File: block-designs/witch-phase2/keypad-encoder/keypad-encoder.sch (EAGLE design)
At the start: 70 parts, among them IC1 74AHC1G14DBV, IC2 74AHC1G14DBV, IC3 74AHC1G14DBV, IC4 74AHC1G14DBV, IC5 74AHC1G14DBV

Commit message: completed schematic with basic pcb layout
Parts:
- removed D26, D28, D30, D31, D32, D33, D34: (no value), SparkFun-DiscreteSemi:DIODEPTH
- removed JP1: (no value), pinhead:PINHD-1X18
- added D1, D2: (no value), SparkFun-DiscreteSemi:DIODEPTH
- added IC6: 74LVC1G17DBV, 74xx-little-us:74LVC1G17DBV
- added IC7: 74LVC1G14DBV, 74xx-little-us:74LVC1G14DBV
- added JP2: (no value), pinhead:PINHD-1X10
- added JP3: (no value), pinhead:PINHD-1X18
- added R17, R18, R19, R20, R21: 1k, resistor:R-US_R0805
- C1, C10, C11, C12, C13, C14, C15, C16, C2, C3, C4, C5, C6, C7, C8, C9: value 10uF -> 0.1uF
- IC1, IC2, IC3, IC4, IC5: value 74AHC1G14DBV -> 74LVC1G17DBV; device 74xx-little-us:74AHC1G14DBV -> 74xx-little-us:74LVC1G17DBV
- R1, R10, R11, R12, R13, R14, R15, R16, R2, R3, R4, R5, R6, R7, R8, R9: value 10k -> 1k
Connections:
- removed net N$10: JP1.9
- removed net N$11: JP1.10
- removed net N$12: JP1.11
- removed net N$13: JP1.12
- removed net N$14: JP1.13
- removed net N$15: JP1.14
- removed net N$16: JP1.15
- removed net N$17: JP1.16
- removed net N$18: JP1.17
- removed net N$2: JP1.1
- removed net N$20: R1.1, R10.1, R11.1, R12.1, R13.1, R14.1, R15.1, R16.1, R2.1, R3.1, R4.1, R5.1, R6.1, R7.1, R8.1, R9.1
- removed net N$3: JP1.2
- removed net N$31: C11.1, D23.A, D24.A, R11.2
- removed net N$37: D11.C, D13.C, D15.C, D17.C, D19.C, D21.C, D23.C, D25.C, D27.C, D29.C, D3.C, D31.C, D33.C, D5.C, D7.C, D9.C
- removed net N$38: D10.C, D12.C, D14.C, D16.C, D18.C, D20.C, D22.C, D24.C, D26.C, D28.C, D30.C, D32.C, D34.C, D4.C, D6.C, D8.C
- removed net N$4: JP1.3
- removed net N$5: JP1.4
- removed net N$6: JP1.5
- removed net N$7: JP1.6
- removed net N$8: JP1.7
- removed net N$9: JP1.8
- new net !RESET: IC7A.O, JP2.8
- new net EXEC: IC6G$1.O, JP2.9
- new net OUT_A: D1.C, D15.C, D17.C, D21.C, D29.C, D3.C, IC1G$1.I, R17.2
- new net OUT_B: D19.C, D22.C, D5.C, D7.C, IC2G$1.I, R18.2
- new net OUT_C: D11.C, D23.C, D25.C, D4.C, D6.C, D9.C, IC3G$1.I, R19.2
- new net OUT_D: D10.C, D13.C, D16.C, D24.C, D8.C, IC4G$1.I, R20.2
- new net OUT_E: D12.C, D14.C, D18.C, D2.C, D20.C, D27.C, IC5G$1.I, R21.2
- new net SIGA: IC1G$1.O, JP2.2
- new net SIGB: IC2G$1.O, JP2.3
- new net SIGC: IC3G$1.O, JP2.4
- new net SIGD: IC4G$1.O, JP2.5
- new net SIGE: IC5G$1.O, JP2.6
- new net SW-EXEC: JP3.15, R15.1
- new net SW-MINUS: JP3.10, R13.1
- new net SW-ORDER: JP3.17, R11.1
- new net SW-PLUS: JP3.2, R14.1
- new net SW-RESET: JP3.14, R16.1
- new net SW-SPACE: JP3.16, R12.1
- new net SW0: JP3.6, R10.1
- new net SW1: JP3.5, R6.1
- new net SW2: JP3.9, R1.1
- new net SW3: JP3.13, R2.1
- new net SW4: JP3.4, R3.1
- new net SW5: JP3.8, R4.1
- new net SW6: JP3.12, R5.1
- new net SW7: JP3.3, R7.1
- new net SW8: JP3.7, R8.1
- new net SW9: JP3.11, R9.1
- new net VCC: JP2.1, JP3.1
- net GND: now also JP2.10, JP3.18, R17.1, R18.1, R19.1, R20.1, R21.1
- net N$1: now also C11.1, D1.A, D2.A, D23.A, D24.A, R11.2; no longer JP1.18
- net N$32: no longer D26.A
- net N$33: no longer D28.A
- net N$34: no longer D30.A
- net N$35: now also IC6G$1.I; no longer D31.A, D32.A
- net N$36: now also IC7A.I; no longer D33.A, D34.A
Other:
- moved on the sheet: C1, C10, C11, C12, C13, C14, C15, C16, C2, C3, C4, C5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

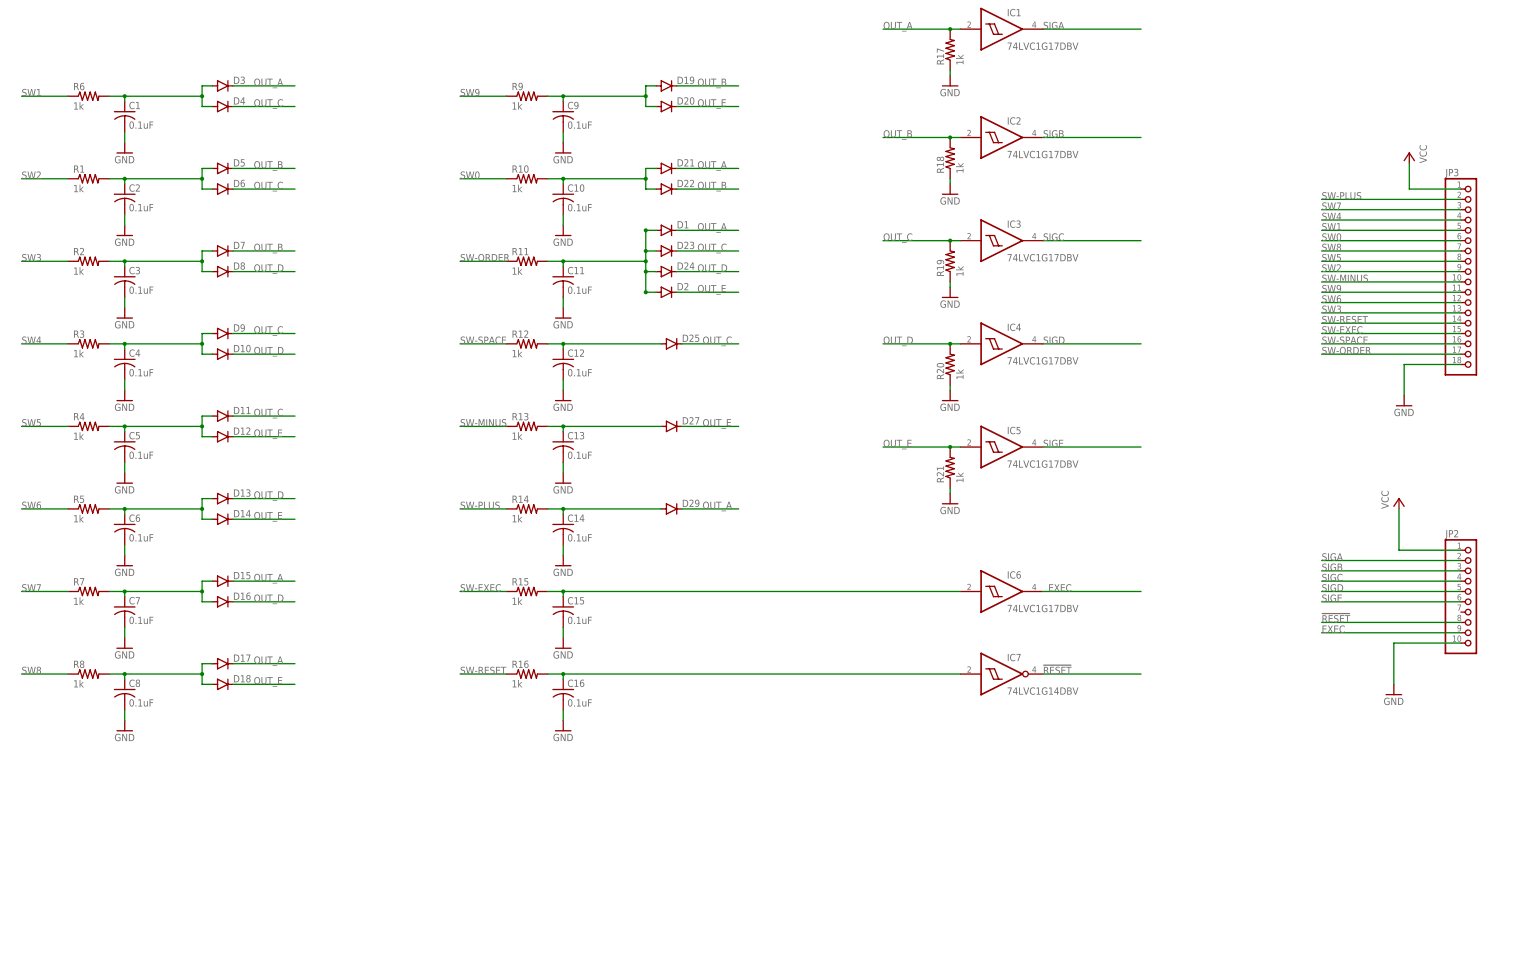
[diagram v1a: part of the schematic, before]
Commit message: reduced size of module and layout cleanup
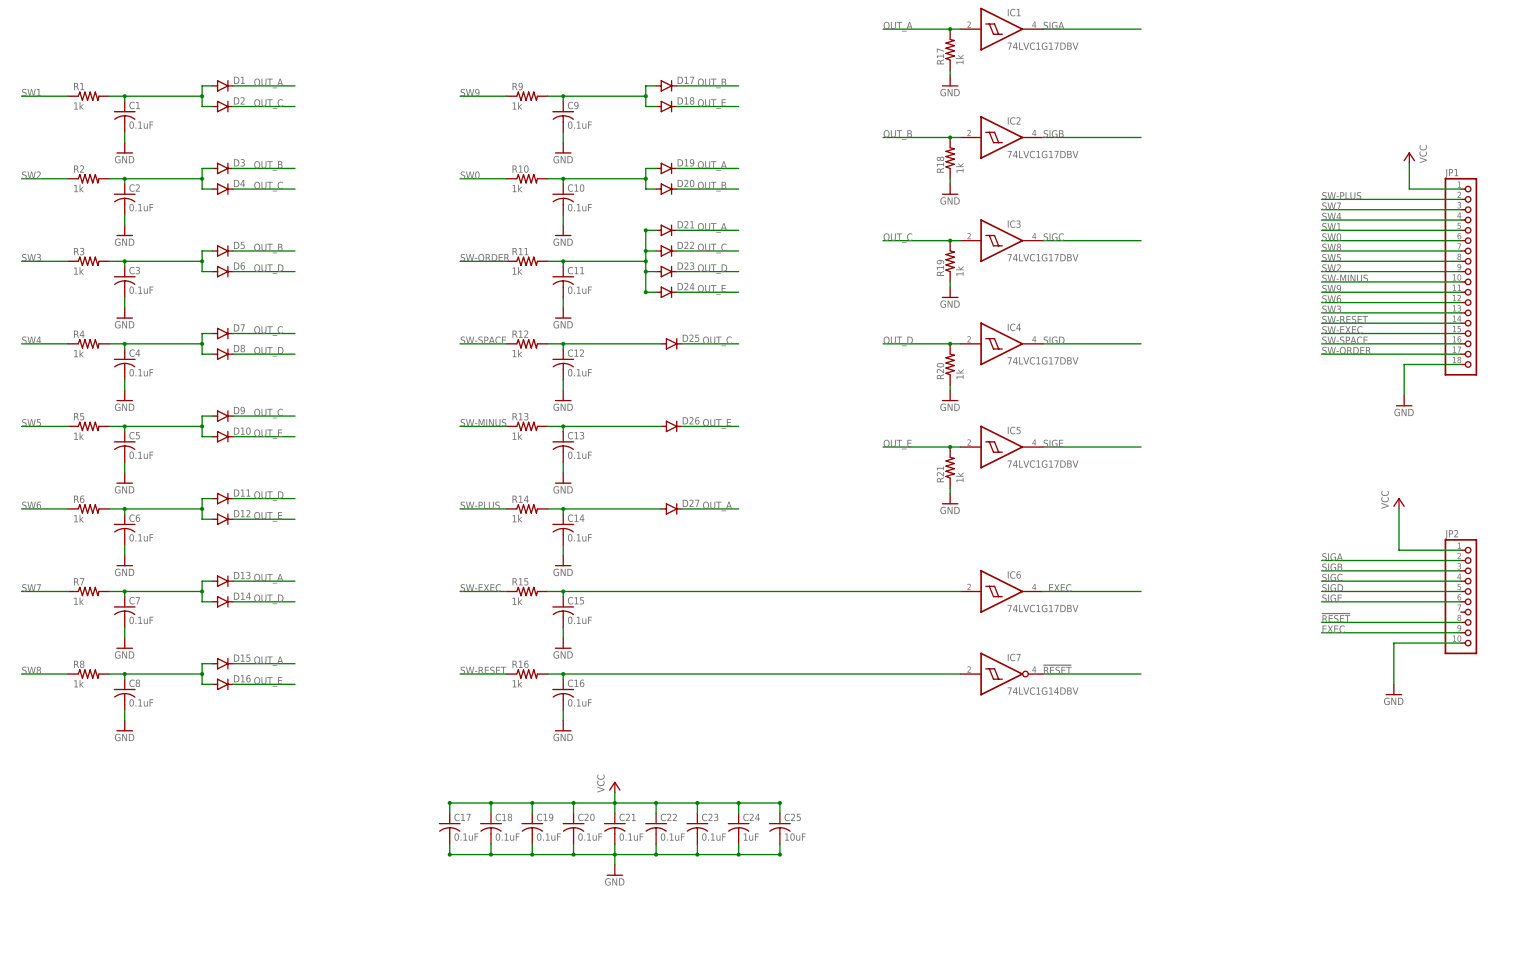
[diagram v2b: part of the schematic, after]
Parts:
- removed D29: (no value), SparkFun-DiscreteSemi:DIODEPTH
- added C17, C18, C19, C20, C21, C22, C23: 0.1uF, resistor:C-USC0805
- added C24: 1uF, resistor:C-USC0805
- added C25: 10uF, resistor:C-USC0805
- added D26: (no value), SparkFun-DiscreteSemi:DIODEPTH
- renumbered JP3 to JP1
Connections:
- net GND: now also C17.2, C18.2, C19.2, C20.2, C21.2, C22.2, C23.2, C24.2, C25.2
- net N$1: now also D21.A, D22.A; no longer D1.A, D2.A
- net N$19: now also D1.A, D2.A, R1.2; no longer D3.A, D4.A, R6.2
- net N$22: now also D3.A, D4.A, R2.2; no longer D5.A, D6.A, R1.2
- net N$23: now also D5.A, D6.A, R3.2; no longer D7.A, D8.A, R2.2
- net N$24: now also D7.A, D8.A, R4.2; no longer D10.A, D9.A, R3.2
- net N$25: now also D10.A, D9.A, R5.2; no longer D11.A, D12.A, R4.2
- net N$26: now also D11.A, D12.A, R6.2; no longer D13.A, D14.A, R5.2
- net N$27: now also D13.A, D14.A; no longer D15.A, D16.A
- net N$28: now also D15.A, D16.A; no longer D17.A, D18.A
- net N$29: now also D17.A, D18.A; no longer D19.A, D20.A
- net N$30: now also D19.A, D20.A; no longer D21.A, D22.A
- net N$33: now also D26.A; no longer D27.A
- net N$34: now also D27.A; no longer D29.A
- net OUT_A: now also D13.C, D19.C, D27.C; no longer D17.C, D29.C, D3.C
- net OUT_B: now also D17.C, D20.C, D3.C; no longer D19.C, D22.C, D7.C
- net OUT_C: now also D2.C, D22.C, D7.C; no longer D11.C, D23.C, D6.C
- net OUT_D: now also D11.C, D14.C, D23.C, D6.C; no longer D10.C, D13.C, D16.C, D24.C
- net OUT_E: now also D10.C, D16.C, D24.C, D26.C; no longer D14.C, D2.C, D20.C, D27.C
- net SW1: now also R1.1; no longer R6.1
- net SW2: now also R2.1; no longer R1.1
- net SW3: now also R3.1; no longer R2.1
- net SW4: now also R4.1; no longer R3.1
- net SW5: now also R5.1; no longer R4.1
- net SW6: now also R6.1; no longer R5.1
- net VCC: now also C17.1, C18.1, C19.1, C20.1, C21.1, C22.1, C23.1, C24.1, C25.1
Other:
- moved on the sheet: D1, D10, D11, D12, D13, D14, D15, D16, D17, D18, D19, D2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

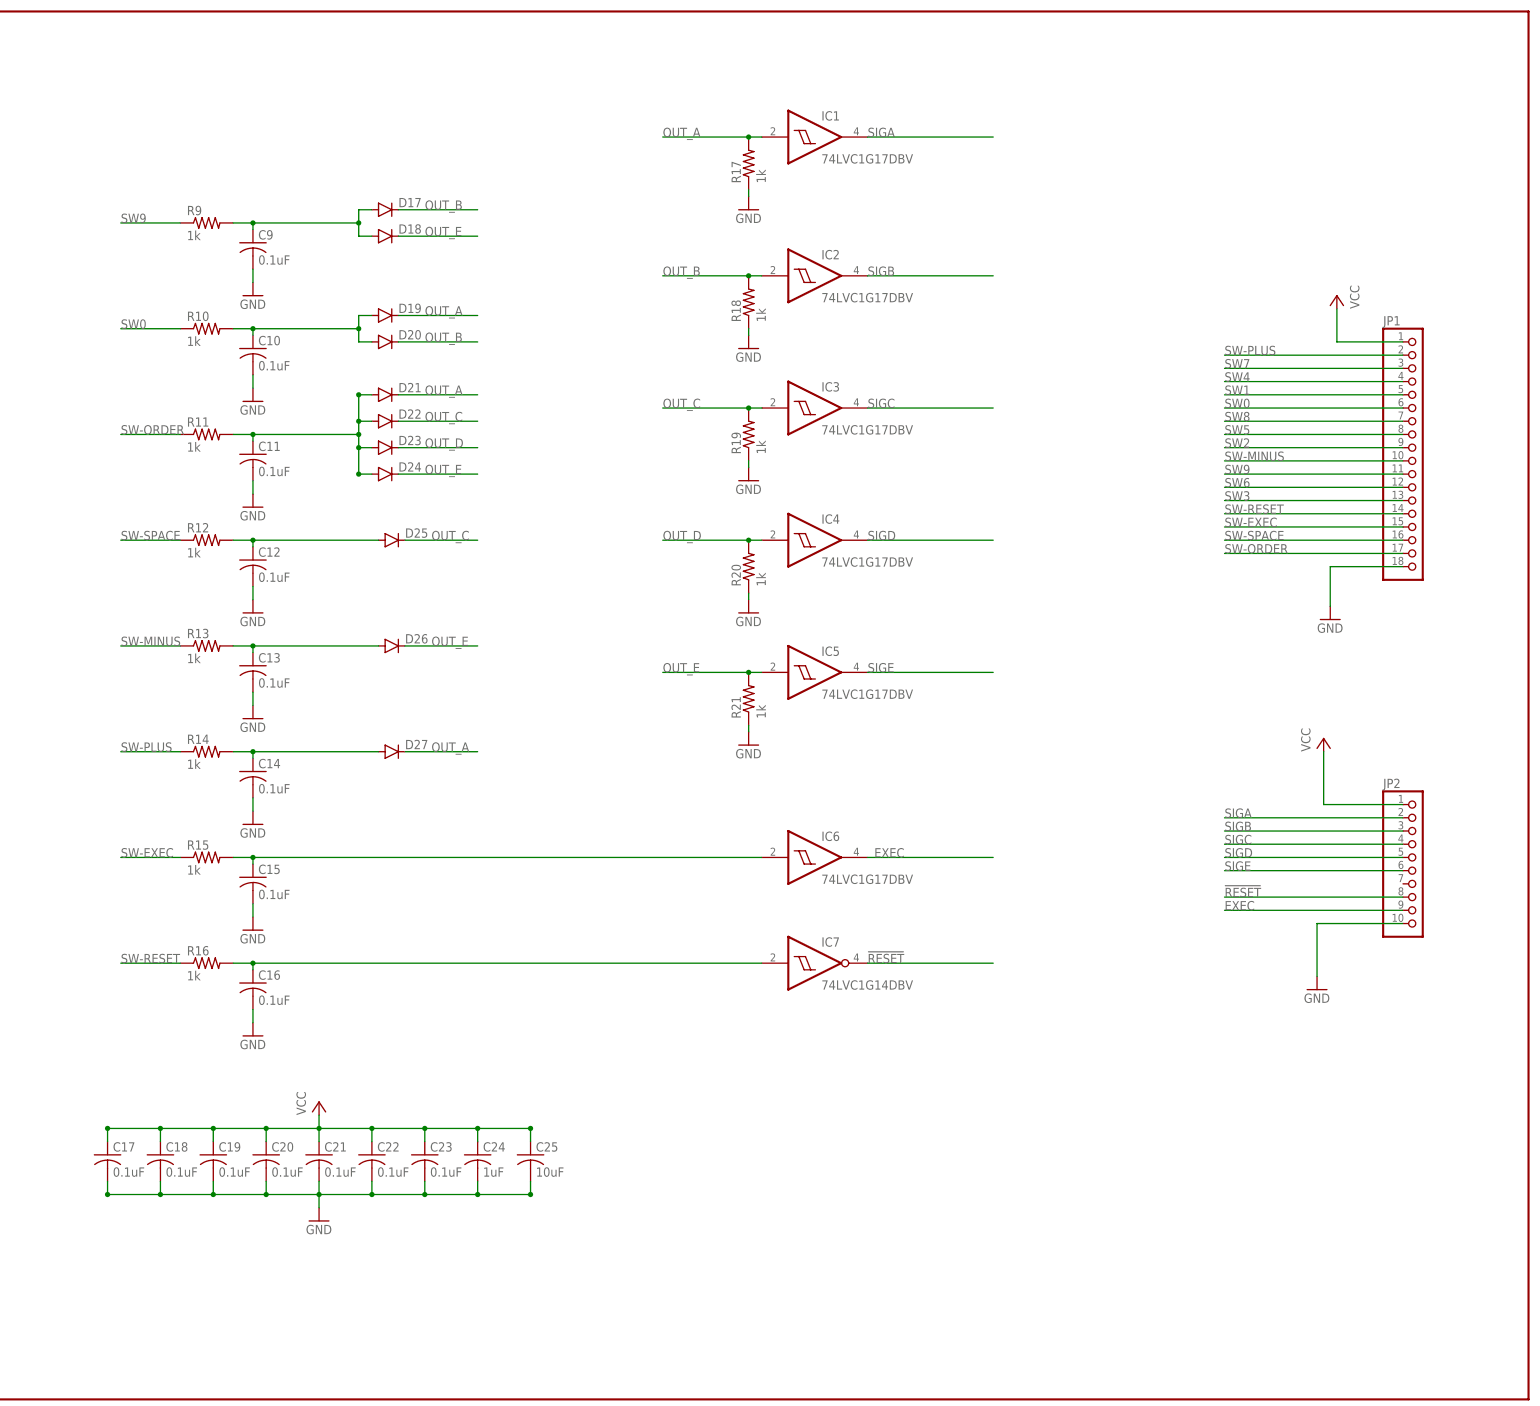
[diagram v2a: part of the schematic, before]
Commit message: rework of cabling for reset, exec, power, and key-up detection
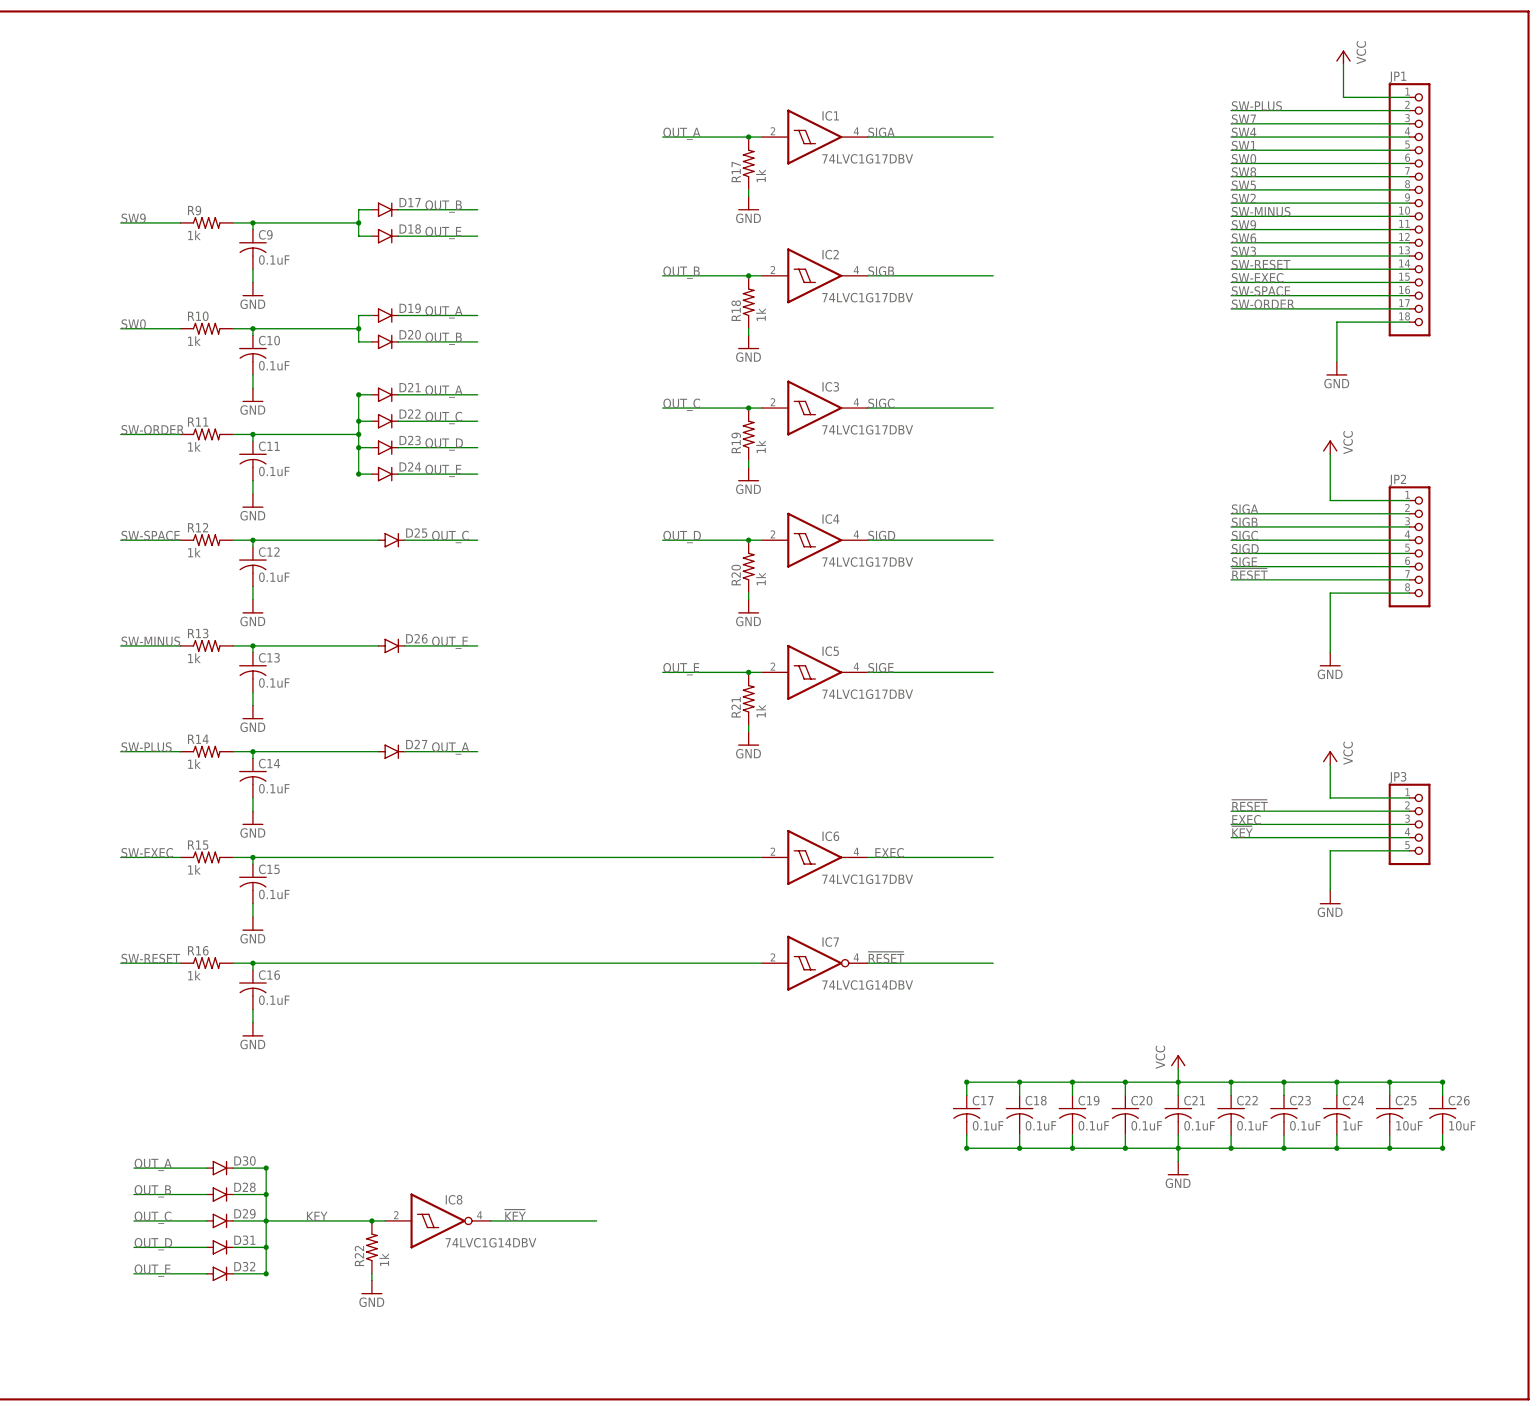
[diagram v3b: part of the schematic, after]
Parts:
- added C26: 10uF, resistor:C-USC0805
- added D28, D29, D30, D31, D32: (no value), SparkFun-DiscreteSemi:DIODEPTH
- added IC8: 74LVC1G14DBV, 74xx-little-us:74LVC1G14DBV
- added JP3: (no value), custom-pinhead:PINHD-1X5
- added R22: 1k, resistor:R-US_R0805
- JP2: device pinhead:PINHD-1X10 -> custom-pinhead:PINHD-1X8
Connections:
- new net !KEY: IC8A.O, JP3.4
- new net KEY: D28.C, D29.C, D30.C, D31.C, D32.C, IC8A.I, R22.2
- net !RESET: now also JP2.7, JP3.2; no longer JP2.8
- net EXEC: now also JP3.3; no longer JP2.9
- net GND: now also C26.2, JP2.8, JP3.5, R22.1; no longer JP2.10
- net OUT_A: now also D30.A
- net OUT_B: now also D28.A
- net OUT_C: now also D29.A
- net OUT_D: now also D31.A
- net OUT_E: now also D32.A
- net VCC: now also C26.1, JP3.1
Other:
- moved on the sheet: C17, C18, C19, C20, C21, C22, C23, C24, C25, JP1
